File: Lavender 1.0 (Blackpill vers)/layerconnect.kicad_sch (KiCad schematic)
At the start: 6 parts, among them J10 Conn_01x13_Pin, J11 Conn_01x13_Pin, J12 Conn_01x13_Pin, J13 Conn_01x13_Pin, J5 Conn_01x28_Pin, J8 Conn_01x28_Pin

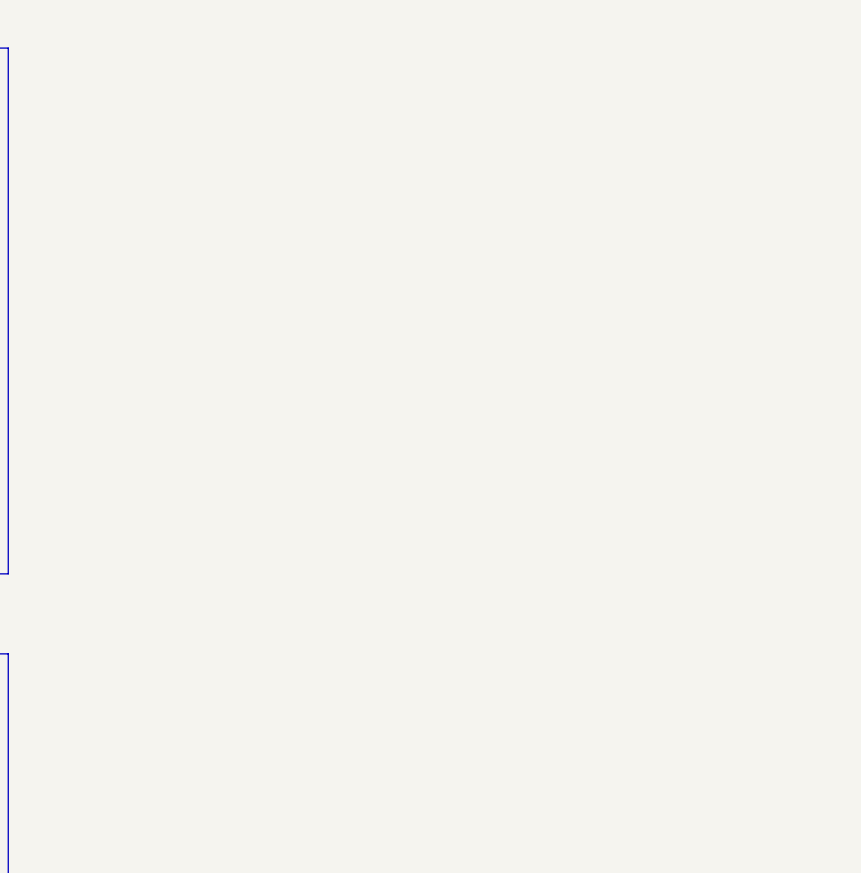
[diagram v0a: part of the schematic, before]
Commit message: Add polyfuse
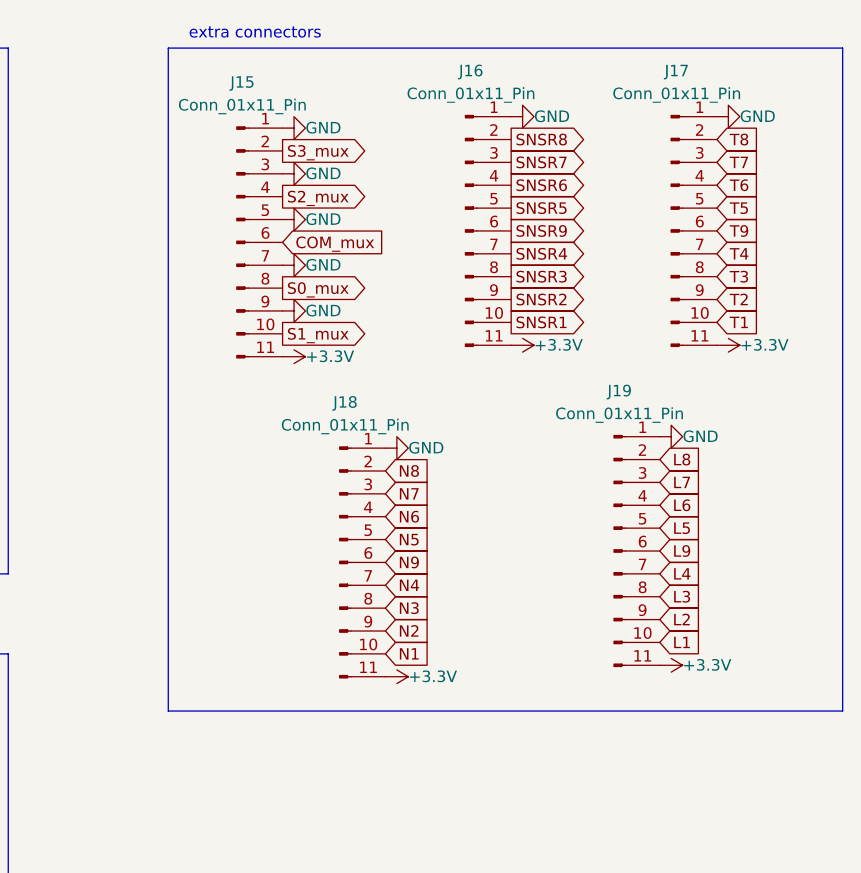
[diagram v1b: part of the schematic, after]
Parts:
- added J15, J16, J17, J18, J19: Conn_01x11_Pin, Connector_PinHeader_2.54mm:PinHeader_1x11_P2.54mm_Vertical, symbol Connector:Conn_01x11_Pin
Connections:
- net +3.3V: now also J15.11 (Pin_11), J16.11 (Pin_11), J17.11 (Pin_11), J18.11 (Pin_11), J19.11 (Pin_11)
- net GND: now also J15.1 (Pin_1), J15.3 (Pin_3), J15.5 (Pin_5), J15.7 (Pin_7), J15.9 (Pin_9), J16.1 (Pin_1), J17.1 (Pin_1), J18.1 (Pin_1), J19.1 (Pin_1)
- new net COM_mux: J15.6 (Pin_6)
- new net L1: J19.10 (Pin_10)
- new net L2: J19.9 (Pin_9)
- new net L3: J19.8 (Pin_8)
- new net L4: J19.7 (Pin_7)
- new net L5: J19.5 (Pin_5)
- new net L6: J19.4 (Pin_4)
- new net L7: J19.3 (Pin_3)
- new net L8: J19.2 (Pin_2)
- new net L9: J19.6 (Pin_6)
- new net N1: J18.10 (Pin_10)
- new net N2: J18.9 (Pin_9)
- new net N3: J18.8 (Pin_8)
- new net N4: J18.7 (Pin_7)
- new net N5: J18.5 (Pin_5)
- new net N6: J18.4 (Pin_4)
- new net N7: J18.3 (Pin_3)
- new net N8: J18.2 (Pin_2)
- new net N9: J18.6 (Pin_6)
- new net S0_mux: J15.8 (Pin_8)
- new net S1_mux: J15.10 (Pin_10)
- new net S2_mux: J15.4 (Pin_4)
- new net S3_mux: J15.2 (Pin_2)
- new net SNSR1: J16.10 (Pin_10)
- new net SNSR2: J16.9 (Pin_9)
- new net SNSR3: J16.8 (Pin_8)
- new net SNSR4: J16.7 (Pin_7)
- new net SNSR5: J16.5 (Pin_5)
- new net SNSR6: J16.4 (Pin_4)
- new net SNSR7: J16.3 (Pin_3)
- new net SNSR8: J16.2 (Pin_2)
- new net SNSR9: J16.6 (Pin_6)
- new net T1: J17.10 (Pin_10)
- new net T2: J17.9 (Pin_9)
- new net T3: J17.8 (Pin_8)
- new net T4: J17.7 (Pin_7)
- new net T5: J17.5 (Pin_5)
- new net T6: J17.4 (Pin_4)
- new net T7: J17.3 (Pin_3)
- new net T8: J17.2 (Pin_2)
- new net T9: J17.6 (Pin_6)
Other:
- note added: "extra connectors"
